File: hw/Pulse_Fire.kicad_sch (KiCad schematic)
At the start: 29 parts, among them J2 Conn_01x04, U1 PY32F003F18U6, U2 SC7A20, U3 FM8002A, U4 ME6206A33XG, U5 WS2913, U6 ME2188A50

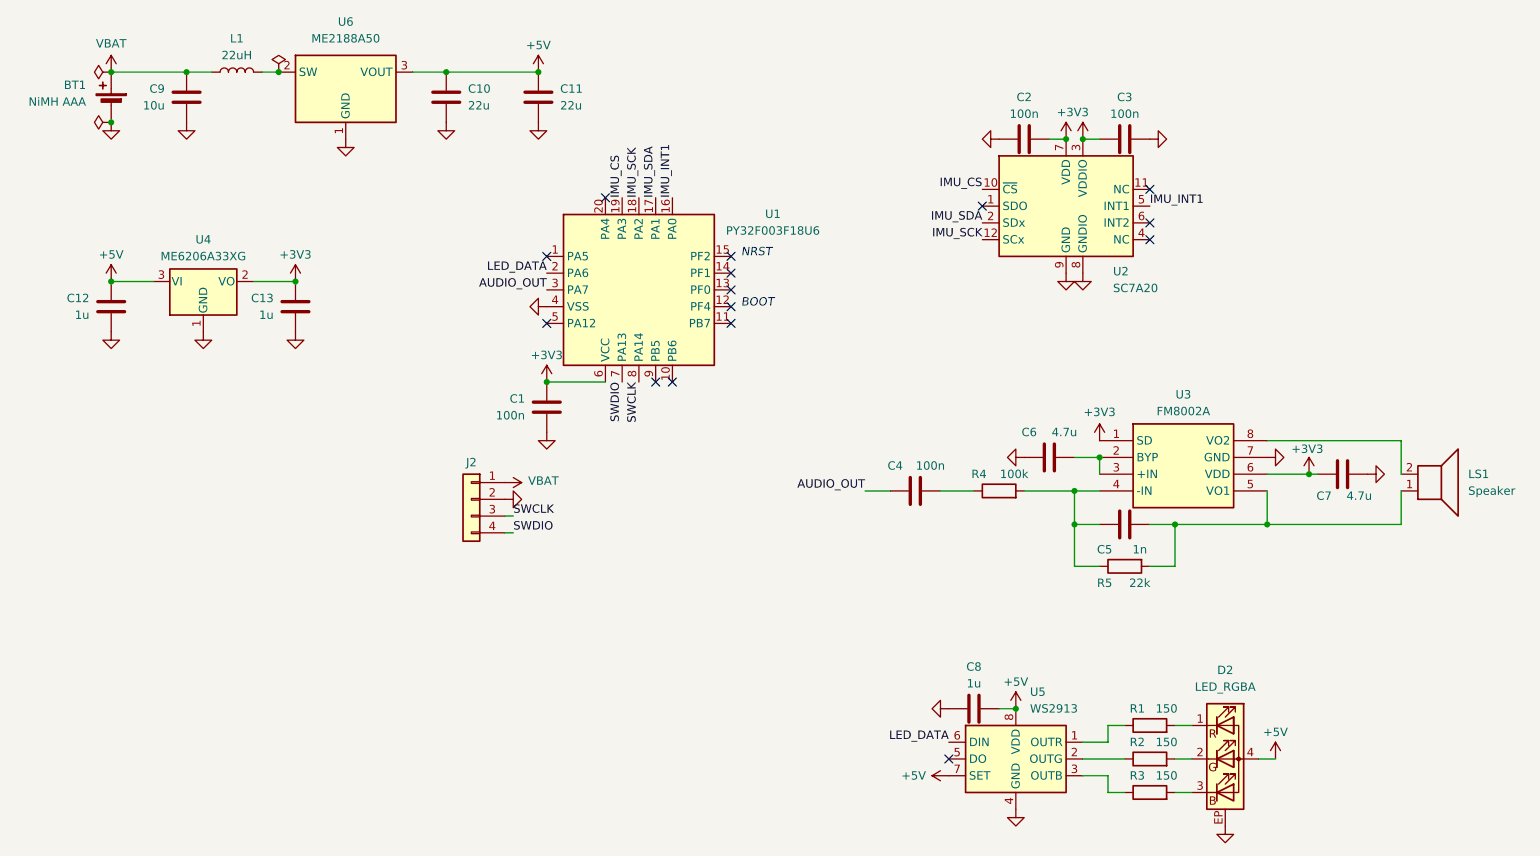
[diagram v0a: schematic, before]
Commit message: hw: Revise schematic to use discrete MOSFETs
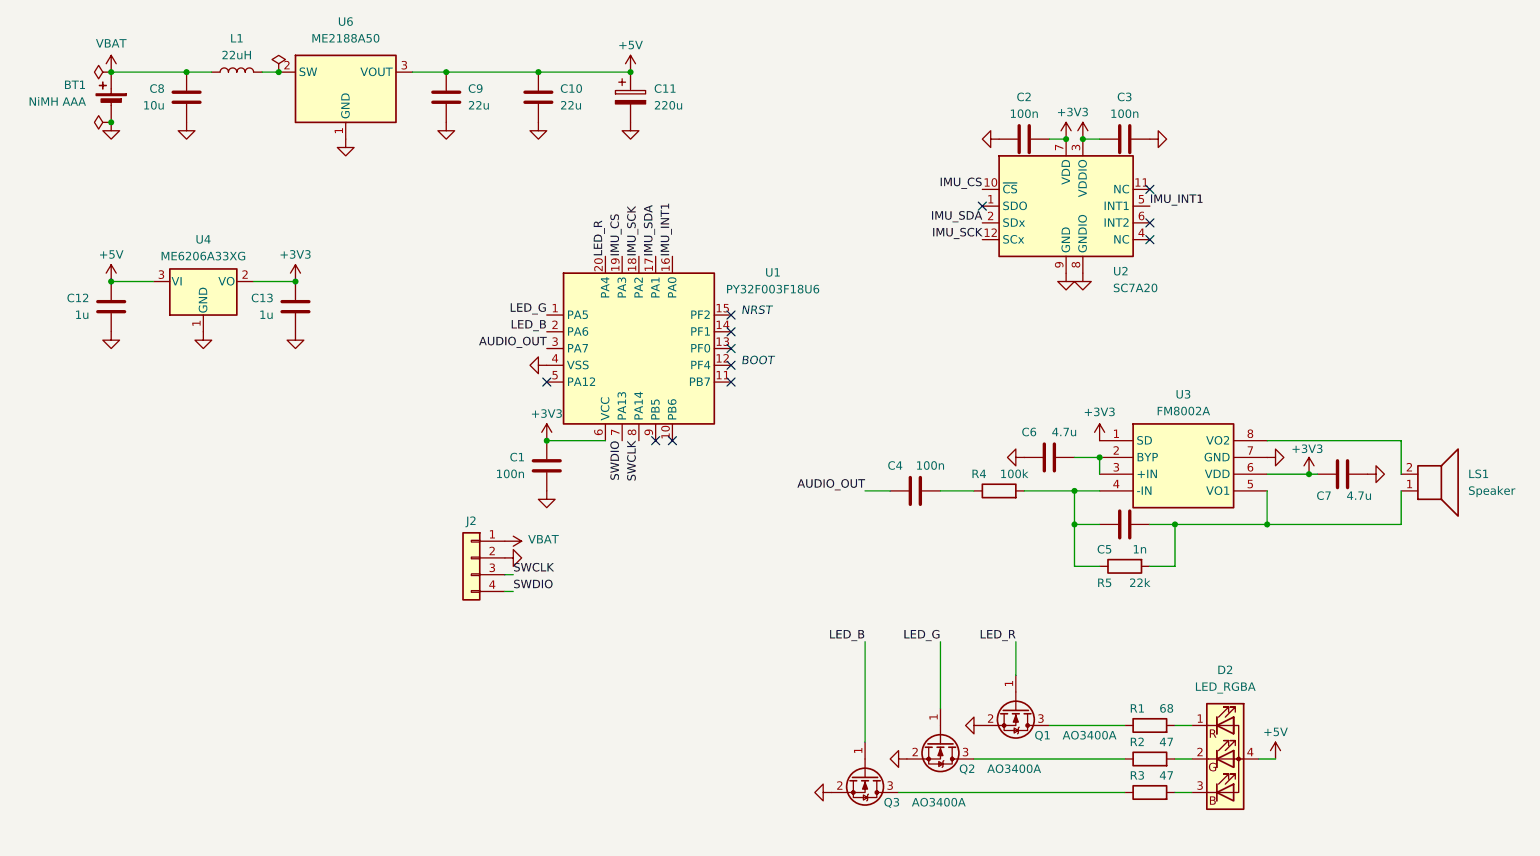
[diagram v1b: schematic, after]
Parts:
- removed C8: 1u, Capacitor_SMD:C_0402_1005Metric, symbol Device:C
- removed U5: WS2913, Package_SO:SOP-8_3.9x4.9mm_P1.27mm, symbol Driver_LED:WS2811
- added C11: 220u, Capacitor_SMD:CP_Elec_6.3x5.4, symbol Device:C_Polarized
- added Q1, Q2, Q3: AO3400A, Package_TO_SOT_SMD:SOT-23, symbol Transistor_FET:AO3400A
- D2: footprint (none) -> Connector_JST:JST_PH_S4B-PH-SM4-TB_1x04-1MP_P2.00mm_Horizontal
- R1: value 150 -> 68
- R2, R3: value 150 -> 47
- renumbered C11 to C10, C9 to C8, C10 to C9
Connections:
- net +5V: now also C11.1
- net GND: now also C11.2, Q1.2 (S), Q2.2 (S), Q3.2 (S); no longer D2.EP
- net LED_G: now reaches U1.1 (PA5)
- net LED_G: now also Q2.1 (G)
- net LED_R: now reaches U1.20 (PA4)
- net LED_R: now also Q1.1 (G)
- net at R1.1: now also Q1.3 (D)
- net at R2.1: now also Q2.3 (D)
- net at R3.1: now also Q3.3 (D)
- net LED_DATA renamed LED_B
- net LED_B: now also Q3.1 (G)
- no-connect marks 15 -> 12
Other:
- moved on the sheet: C1, J2, U1

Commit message: hw: Schematic -- add mounting pins for JST connectors
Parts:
- LS1: footprint Pulse_footprints:Pads_P2.00 -> Connector_JST:JST_PH_S2B-PH-SM4-TB_1x02-1MP_P2.00mm_Horizontal
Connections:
- net +5V: now also J2.1 (Pin_1)
- net GND: now also D2.MP, LS1.MP
- net VBAT: no longer J2.1 (Pin_1)
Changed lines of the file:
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@@
 	)
 	(symbol
+		(lib_id "power:GND")
+		(at 228.6 95.25 0)
+		(unit 1)
+		(exclude_from_sim no)
+		(in_bom yes)
+		(on_board yes)
+		(dnp no)
+		(fields_autoplaced yes)
+		(property "Reference" "#PWR032"
+			(at 228.6 101.6 0)
+			(effects
+				(font
+					(size 1.27 1.27)
+				)
+				(hide yes)
+			)
+		)
+		(property "Value" "GND"
+			(at 228.6 100.33 0)
+			(effects
+				(font
+					(size 1.27 1.27)
+				)
+				(hide yes)
+			)
+		)
+		(property "Footprint" ""
+			(at 228.6 95.25 0)
+			(effects
+				(font
+					(size 1.27 1.27)
+				)
+				(hide yes)
+			)
+		)
+		(property "Datasheet" ""
+			(at 228.6 95.25 0)
+			(effects
+				(font
+					(size 1.27 1.27)
+				)
+				(hide yes)
+			)
+		)
+		(property "Description" "Power symbol creates a global label with name \"GND\" , ground"
+			(at 228.6 95.25 0)
+			(effects
+				(font
+					(size 1.27 1.27)
+				)
+				(hide yes)
+			)
+		)
+		(pin "1"
+		)
+		(instances
+			(project "Pulse_Fire"
+				(path "/49429a57-8612-48d8-83b1-7633b6997710"
+					(reference "#PWR032")
+					(unit 1)
+				)
+			)
+		)
+	)
+	(symbol
 		(lib_id "Device:C")
 		(at 27.94 62.23 180)
@@
 		(pin "3"
 		)
+		(pin "MP"
+		)
 		(instances
 			(project ""
@@
 			)
 		)
-		(property "Footprint" "Pulse_footprints:Pads_P2.00"
+		(property "Footprint" "Connector_JST:JST_PH_S2B-PH-SM4-TB_1x02-1MP_P2.00mm_Horizontal"
 			(at 228.6 85.09 0)
 			(effects
@@
 		(pin "2"
 		)
+		(pin "MP"
+		)
 		(instances
 			(project ""
@@
 	)
 	(symbol
+		(lib_id "power:+5V")
+		(at 87.63 97.79 270)
+		(unit 1)
+		(exclude_from_sim no)
+		(in_bom yes)
+		(on_board yes)
+		(dnp no)
+		(property "Reference" "#PWR09"
+			(at 83.82 97.79 0)
+			(effects
+				(font
+					(size 1.27 1.27)
+				)
+				(hide yes)
+			)
+		)
+		(property "Value" "+5V"
+			(at 92.964 97.536 90)
+			(effects
+				(font
+					(size 1.27 1.27)
+				)
+			)
+		)
+		(property "Footprint" ""
+			(at 87.63 97.79 0)
+			(effects
+				(font
+					(size 1.27 1.27)
+				)
+				(hide yes)
+			)
+		)
+		(property "Datasheet" ""
+			(at 87.63 97.79 0)
+			(effects
+				(font
+					(size 1.27 1.27)
+				)
+				(hide yes)
+			)
+		)
+		(property "Description" "Power symbol creates a global label with name \"+5V\""
+			(at 87.63 97.79 0)
+			(effects
+				(font
+					(size 1.27 1.27)
+				)
+				(hide yes)
+			)
+		)
+		(pin "1"
+		)
+		(instances
+			(project "Pulse_Fire"
+				(path "/49429a57-8612-48d8-83b1-7633b6997710"
+					(reference "#PWR09")
+					(unit 1)
+				)
+			)
+		)
+	)
+	(symbol
 		(lib_id "Device:R")
 		(at 185.42 130.81 90)
@@
 	(symbol
 		(lib_id "power:GND")
+		(at 196.85 140.97 0)
+		(unit 1)
+		(exclude_from_sim no)
+		(in_bom yes)
+		(on_board yes)
+		(dnp no)
+		(fields_autoplaced yes)
+		(property "Reference" "#PWR041"
+			(at 196.85 147.32 0)
+			(effects
+				(font
+					(size 1.27 1.27)
+				)
+				(hide yes)
+			)
+		)
+		(property "Value" "GND"
+			(at 196.85 146.05 0)
+			(effects
+				(font
+					(size 1.27 1.27)
+				)
+				(hide yes)
+			)
+		)
+		(property "Footprint" ""
+			(at 196.85 140.97 0)
+			(effects
+				(font
+					(size 1.27 1.27)
+				)
+				(hide yes)
+			)
+		)
+		(property "Datasheet" ""
+			(at 196.85 140.97 0)
+			(effects
+				(font
+					(size 1.27 1.27)
+				)
+				(hide yes)
+			)
+		)
+		(property "Description" "Power symbol creates a global label with name \"GND\" , ground"
+			(at 196.85 140.97 0)
+			(effects
+				(font
+					(size 1.27 1.27)
+				)
+				(hide yes)
+			)
+		)
+		(pin "1"
+		)
+		(instances
+			(project "Pulse_Fire"
+				(path "/49429a57-8612-48d8-83b1-7633b6997710"
+					(reference "#PWR041")
+					(unit 1)
+				)
+			)
+		)
+	)
+	(symbol
+		(lib_id "power:GND")
 		(at 92.71 34.29 0)
 		(unit 1)
@@
 					(unit 1)
 				)
-			)
-		)
-	)
-	(symbol
-		(lib_name "VBUS_1")
-		(lib_id "power:VBUS")
-		(at 87.63 97.79 270)
-		(unit 1)
-		(exclude_from_sim no)
-		(in_bom yes)
-		(on_board yes)
-		(dnp no)
-		(property "Reference" "#PWR049"
-			(at 83.82 97.79 0)
-			(effects
-				(font
-					(size 1.27 1.27)
-				)
-				(hide yes)
-			)
-		)
-		(property "Value" "VBAT"
-			(at 93.472 97.536 90)
-			(effects
-				(font
-					(size 1.27 1.27)
-				)
-			)
-		)
-		(property "Footprint" ""
-			(at 87.63 97.79 0)
-			(effects
-				(font
-					(size 1.27 1.27)
-				)
-				(hide yes)
-			)
-		)
-		(property "Datasheet" ""
-			(at 87.63 97.79 0)
-			(effects
-				(font
-					(size 1.27 1.27)
-				)
-				(hide yes)
-			)
-		)
-		(property "Description" "Power symbol creates a global label with name \"VBUS\""
-			(at 87.63 97.79 0)
-			(effects
-				(font
-					(size 1.27 1.27)
-				)
-				(hide yes)
-			)
-		)
-		(pin "1"
-		)
-		(instances
-			(project "Pulse_Wind"
-				(path "/49429a57-8612-48d8-83b1-7633b6997710"
-					(reference "#PWR049")
-					(unit 1)
-				)

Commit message: hw: Complete board design
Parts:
- R1, R2, R3: footprint Resistor_SMD:R_0402_1005Metric -> Resistor_SMD:R_0603_1608Metric
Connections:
- net +3V3: no longer U3.1 (SD)
- net AUDIO_SD: now reaches U1.5 (PA12)
- net AUDIO_SD: now also U3.1 (SD)
- no-connect marks 12 -> 11
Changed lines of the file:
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@@
 	)
 	(no_connect
-		(at 93.98 73.66)
-	)
-	(no_connect
 		(at 121.92 73.66)
 	)
@@
 	(wire
 		(pts
+			(xy 177.8 78.74) (xy 177.8 82.55)
+		)
+		(stroke
+			(width 0)
+			(type default)
+		)
+	)
+	(wire
+		(pts
 			(xy 173.99 101.6) (xy 173.99 95.25)
 		)
@@
 		)
 	)
+	(label "AUDIO_SD"
+		(at 93.98 73.66 180)
+		(effects
+			(font
+				(size 1.27 1.27)
+			)
+			(justify right bottom)
+		)
+	)
 	(label "IMU_CS"
 		(at 105.41 54.61 90)
@@
 		)
 	)
+	(label "AUDIO_SD"
+		(at 177.8 78.74 180)
+		(effects
+			(font
+				(size 1.27 1.27)
+			)
+			(justify right bottom)
+		)
+	)
 	(label "AUDIO_OUT"
 		(at 142.24 90.17 180)
@@
 			)
 		)
-		(property "Footprint" "Resistor_SMD:R_0402_1005Metric"
+		(property "Footprint" "Resistor_SMD:R_0603_1608Metric"
 			(at 185.42 127.508 90)
 			(effects
@@
 	)
 	(symbol
-		(lib_id "power:+3V3")
-		(at 177.8 82.55 0)
-		(unit 1)
-		(exclude_from_sim no)
-		(in_bom yes)
-		(on_board yes)
-		(dnp no)
-		(property "Reference" "#PWR030"
-			(at 177.8 86.36 0)
-			(effects
-				(font
-					(size 1.27 1.27)
-				)
-				(hide yes)
-			)
-		)
-		(property "Value" "+3V3"
-			(at 177.8 78.232 0)
-			(effects
-				(font
-					(size 1.27 1.27)
-				)
-			)
-		)
-		(property "Footprint" ""
-			(at 177.8 82.55 0)
-			(effects
-				(font
-					(size 1.27 1.27)
-				)
-				(hide yes)
-			)
-		)
-		(property "Datasheet" ""
-			(at 177.8 82.55 0)
-			(effects
-				(font
-					(size 1.27 1.27)
-				)
-				(hide yes)
-			)
-		)
-		(property "Description" ""
-			(at 177.8 82.55 0)
-			(effects
-				(font
-					(size 1.27 1.27)
-				)
-			)
-		)
-		(pin "1"
-		)
-		(instances
-			(project "Pulse_Wind"
-				(path "/49429a57-8612-48d8-83b1-7633b6997710"
-					(reference "#PWR030")
-					(unit 1)
-				)
-			)
-		)
-	)
-	(symbol
 		(lib_id "power:GND")
 		(at 203.2 85.09 90)
@@
 			)
 		)
-		(property "Footprint" "Resistor_SMD:R_0402_1005Metric"
+		(property "Footprint" "Resistor_SMD:R_0603_1608Metric"
 			(at 185.42 132.588 90)
 			(effects
@@
 			)
 		)
-		(property "Footprint" "Resistor_SMD:R_0402_1005Metric"
+		(property "Footprint" "Resistor_SMD:R_0603_1608Metric"
 			(at 185.42 137.668 90)
 			(effects

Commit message: hw: Place silkscreen
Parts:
- renumbered D2 to D1, J2 to J1, U6 to U4, U4 to U5
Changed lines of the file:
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@@
 		(on_board yes)
 		(dnp no)
-		(property "Reference" "J2"
+		(property "Reference" "J1"
 			(at 82.55 94.742 0)
 			(effects
@@
 			(project "Pulse_Wind"
 				(path "/49429a57-8612-48d8-83b1-7633b6997710"
-					(reference "J2")
+					(reference "J1")
 					(unit 1)
 				)
@@
 		(on_board yes)
 		(dnp no)
-		(property "Reference" "D2"
+		(property "Reference" "D1"
 			(at 196.85 117.348 0)
 			(effects
@@
 			(project ""
 				(path "/49429a57-8612-48d8-83b1-7633b6997710"
-					(reference "D2")
+					(reference "D1")
 					(unit 1)
 				)
@@
 		(dnp no)
 		(fields_autoplaced yes)
-		(property "Reference" "U6"
+		(property "Reference" "U4"
 			(at 63.5 19.05 0)
 			(effects
@@
 			(project ""
 				(path "/49429a57-8612-48d8-83b1-7633b6997710"
-					(reference "U6")
+					(reference "U4")
 					(unit 1)
 				)
@@
 		(dnp no)
 		(fields_autoplaced yes)
-		(property "Reference" "U4"
+		(property "Reference" "U5"
 			(at 41.91 52.07 0)
 			(effects
@@
 			(project "Pulse_Wind"
 				(path "/49429a57-8612-48d8-83b1-7633b6997710"
-					(reference "U4")
+					(reference "U5")
 					(unit 1)
 				)
